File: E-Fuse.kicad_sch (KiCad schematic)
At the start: 19 parts, among them J3 Power Input, J4 5V, J5 5V, J6 5V, J7 1-18V, J8 1-18V, J9 1-18V, U4 TPS16630PWPR

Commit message: hid test points from bom
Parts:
- TPGND2, TPUVLO1: now left out of the parts list
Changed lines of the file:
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@@
 		(body_style 1)
 		(exclude_from_sim no)
-		(in_bom yes)
+		(in_bom no)
 		(on_board yes)
 		(in_pos_files yes)
@@
 		(in_bom yes)
 		(on_board yes)
-		(in_pos_files yes)
+		(in_pos_files no)
 		(dnp no)
 		(property "Reference" "TP1-18"
@@
 		(body_style 1)
 		(exclude_from_sim no)
-		(in_bom yes)
+		(in_bom no)
 		(on_board yes)
 		(in_pos_files yes)

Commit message: routing done
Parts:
- TP1-18: now left out of the parts list
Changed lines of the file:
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@@
 		(body_style 1)
 		(exclude_from_sim no)
-		(in_bom yes)
+		(in_bom no)
 		(on_board yes)
-		(in_pos_files no)
+		(in_pos_files yes)
 		(dnp no)
 		(property "Reference" "TP1-18"

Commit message: updates to BOM
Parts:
- Cin2, Cout1, Cout2: Digikey 1276-6698-1-ND -> 490-10748-1-ND; MPN CL21X106KAYNNNE -> GRM21BR61E106MA73L; Manufacturer Samsung Electro-Mechanics -> Murata Electronics
- R.1: value 150k -> 160k
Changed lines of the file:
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@@
 			)
 		)
-		(property "Value" "150k"
+		(property "Value" "160k"
 			(at 64.262 94.996 0)
 			(show_name no)
@@
 			)
 		)
-		(property "Digikey" "1276-6698-1-ND"
+		(property "Digikey" "490-10748-1-ND"
 			(at 129.54 92.71 0)
 			(hide yes)
@@
 			)
 		)
-		(property "MPN" "CL21X106KAYNNNE"
+		(property "MPN" "GRM21BR61E106MA73L"
 			(at 129.54 92.71 0)
 			(hide yes)
@@
 			)
 		)
-		(property "Manufacturer" "Samsung Electro-Mechanics"
+		(property "Manufacturer" "Murata Electronics"
 			(at 129.54 92.71 0)
 			(hide yes)
@@
 			)
 		)
-		(property "Digikey" "1276-6698-1-ND"
+		(property "Digikey" "490-10748-1-ND"
 			(at 48.26 90.17 0)
 			(hide yes)
@@
 			)
 		)
-		(property "MPN" "CL21X106KAYNNNE"
+		(property "MPN" "GRM21BR61E106MA73L"
 			(at 48.26 90.17 0)
 			(hide yes)
@@
 			)
 		)
-		(property "Manufacturer" "Samsung Electro-Mechanics"
+		(property "Manufacturer" "Murata Electronics"
 			(at 48.26 90.17 0)
 			(hide yes)
@@
 			)
 		)
-		(property "Digikey" "1276-6698-1-ND"
+		(property "Digikey" "490-10748-1-ND"
 			(at 124.46 92.71 0)
 			(hide yes)
@@
 			)
 		)
-		(property "MPN" "CL21X106KAYNNNE"
+		(property "MPN" "GRM21BR61E106MA73L"
 			(at 124.46 92.71 0)
 			(hide yes)
@@
 			)
 		)
-		(property "Manufacturer" "Samsung Electro-Mechanics"
+		(property "Manufacturer" "Murata Electronics"
 			(at 124.46 92.71 0)
 			(hide yes)

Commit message: Change routing to include l2 power layer to rearrange buck layout
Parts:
- J3: footprint Connector_AMASS:AMASS_XT60IPW-M_1x03_P7.20mm_Horizontal -> LEOS:AMASS_XT60IPW-M_1x03_P7.20mm_Horizontal
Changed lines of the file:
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@@
 			)
 		)
-		(property "Footprint" "Connector_AMASS:AMASS_XT60IPW-M_1x03_P7.20mm_Horizontal"
+		(property "Footprint" "LEOS:AMASS_XT60IPW-M_1x03_P7.20mm_Horizontal"
 			(at 168.91 101.6 0)
 			(hide yes)

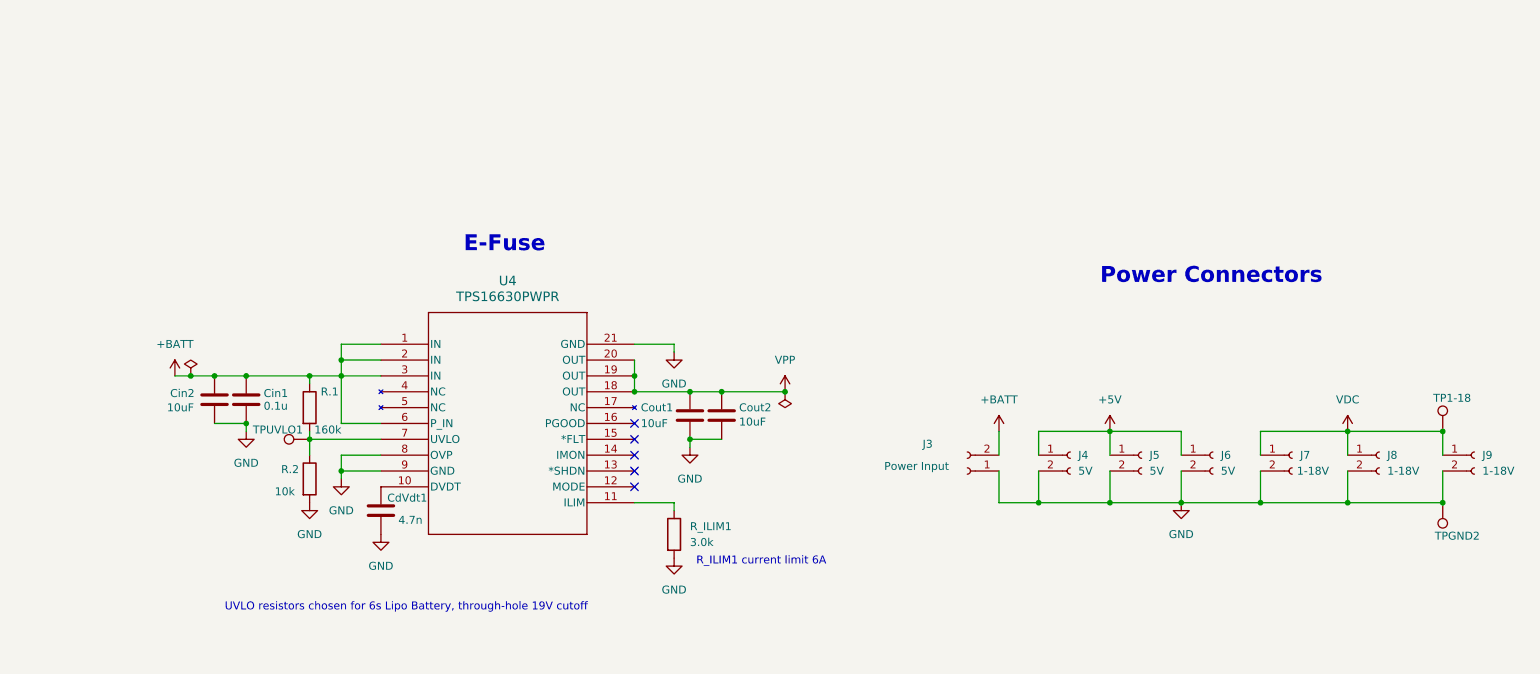
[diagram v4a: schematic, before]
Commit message: Rename references, update symbols and schematic layout
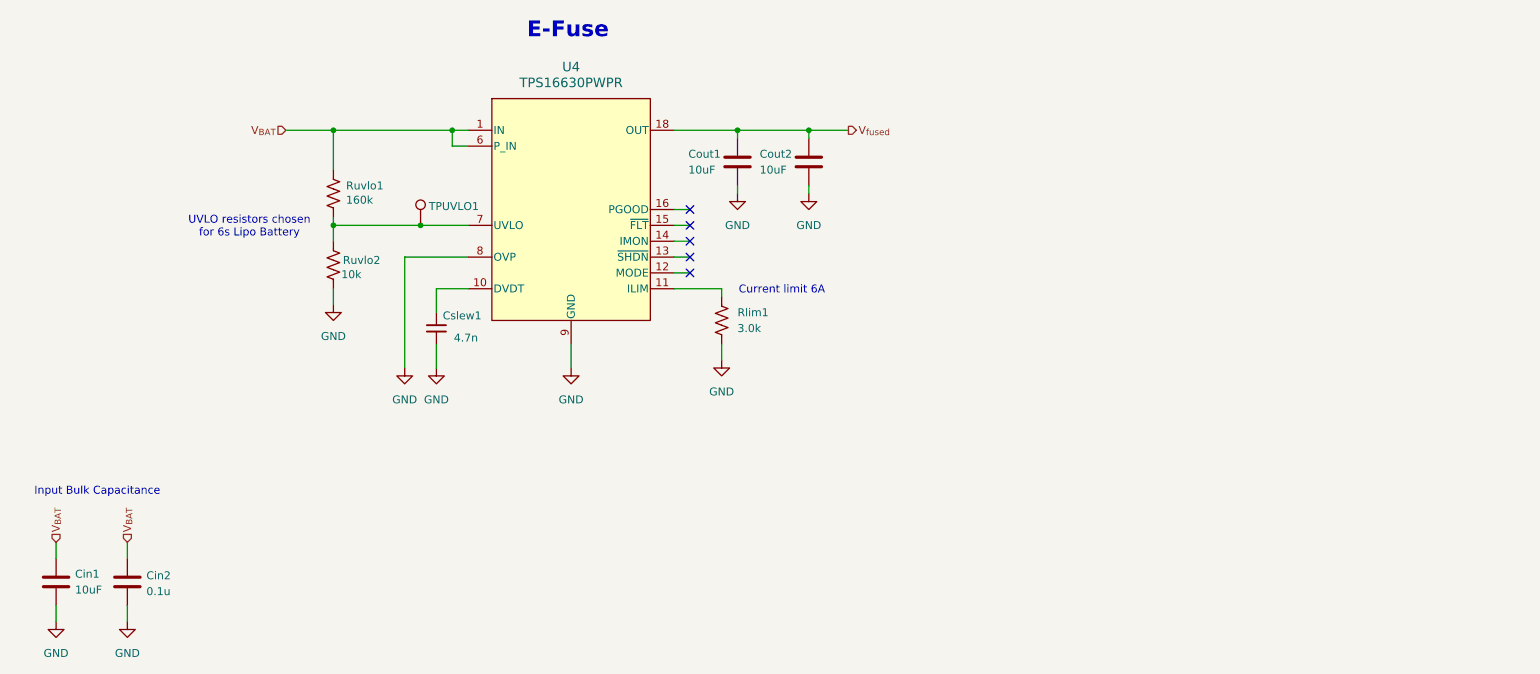
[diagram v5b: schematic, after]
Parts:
- removed J3: Power Input, LEOS:AMASS_XT60IPW-M_1x03_P7.20mm_Horizontal, symbol Connector:Conn_01x02_Socket
- removed J4, J5, J6: 5V, Connector_JST:JST_XH_S2B-XH-A_1x02_P2.50mm_Horizontal, symbol Connector:Conn_01x02_Socket
- removed J7, J8, J9: 1-18V, Connector_JST:JST_XH_S2B-XH-A_1x02_P2.50mm_Horizontal, symbol Connector:Conn_01x02_Socket
- removed TP1-18: TestPoint, TestPoint:TestPoint_Loop_D2.60mm_Drill0.9mm_Beaded, symbol Connector:TestPoint
- removed TPGND2: GND TestPoint, TestPoint:TestPoint_Loop_D2.60mm_Drill0.9mm_Beaded, symbol Connector:TestPoint
- Cin1: value 0.1u -> 10uF; Digikey 1276-1003-1-ND -> 490-10748-1-ND; LCSC C1711 -> (none); MPN CL21B104KBCNNNC -> GRM21BR61E106MA73L; Manufacturer Samsung Electro-Mechanics -> Murata Electronics
- Cin2: value 10uF -> 0.1u; Digikey 490-10748-1-ND -> 1276-1003-1-ND; LCSC (none) -> C1711; MPN GRM21BR61E106MA73L -> CL21B104KBCNNNC; Manufacturer Murata Electronics -> Samsung Electro-Mechanics
- Cslew1: renamed from CdVdt1; symbol Device:C -> Device:C_Small
- Rlim1: renamed from R_ILIM1; symbol Device:R -> Device:R_US
- Ruvlo1: renamed from R.1; symbol Device:R -> Device:R_US
- Ruvlo2: renamed from R.2; symbol Device:R -> Device:R_US
- U4: symbol 2026-09-04_17-36-40:TPS16630PWPR -> LEOS:TPS16630PWPR
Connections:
- net +BATT renamed V_{BAT}
- net VPP renamed V_{fused}
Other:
- note added: "Current limit 6A"
- note added: "Input Bulk Capacitance"
- note added: "UVLO resistors chosen for 6s Lipo Battery"
- note removed: "Power Connectors"
- note removed: "R_ILIM1 current limit 6A"
- note removed: "UVLO resistors chosen for 6s Lipo Battery, through-hole 19V cutoff"
- company: (none) -> VIP Lightning From the Edge of Space
- moved on the sheet: Cslew1, TPUVLO1
